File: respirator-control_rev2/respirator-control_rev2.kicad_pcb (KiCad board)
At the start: 2 copper layers, 152 x 152.5 mm, 36 parts, among them J1 Conn_01x02, J2 Header 1X4, J3 Header 1X3, J4 Header 1X3, J5 Header 1X4, J6 Header 1X30, SW1 SW_Push_Dual, SW2 SW_Push, SW3 SW_Push_Dual, U1 LCD-016N002L

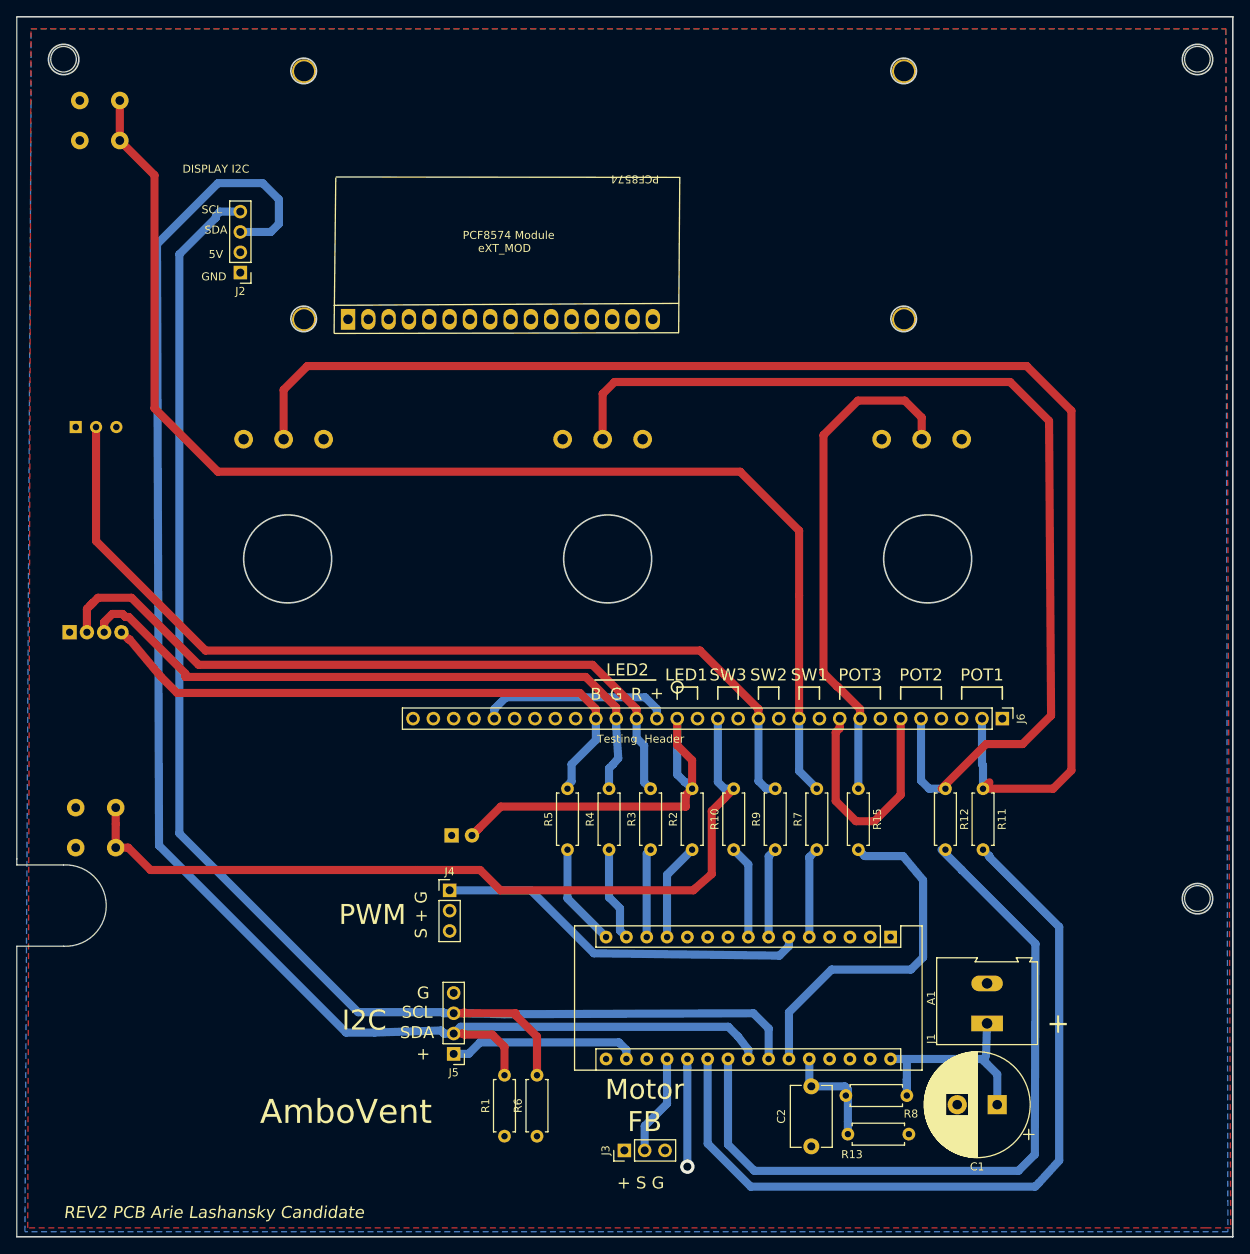
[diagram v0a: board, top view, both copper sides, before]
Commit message: Add files via upload
Change Connectors to horizontal from veritical add Point To secure Cables .
add JPG to Sch to show How to secure Cables.

Gerber in Not Updated  and Not Checked In Fusion  .
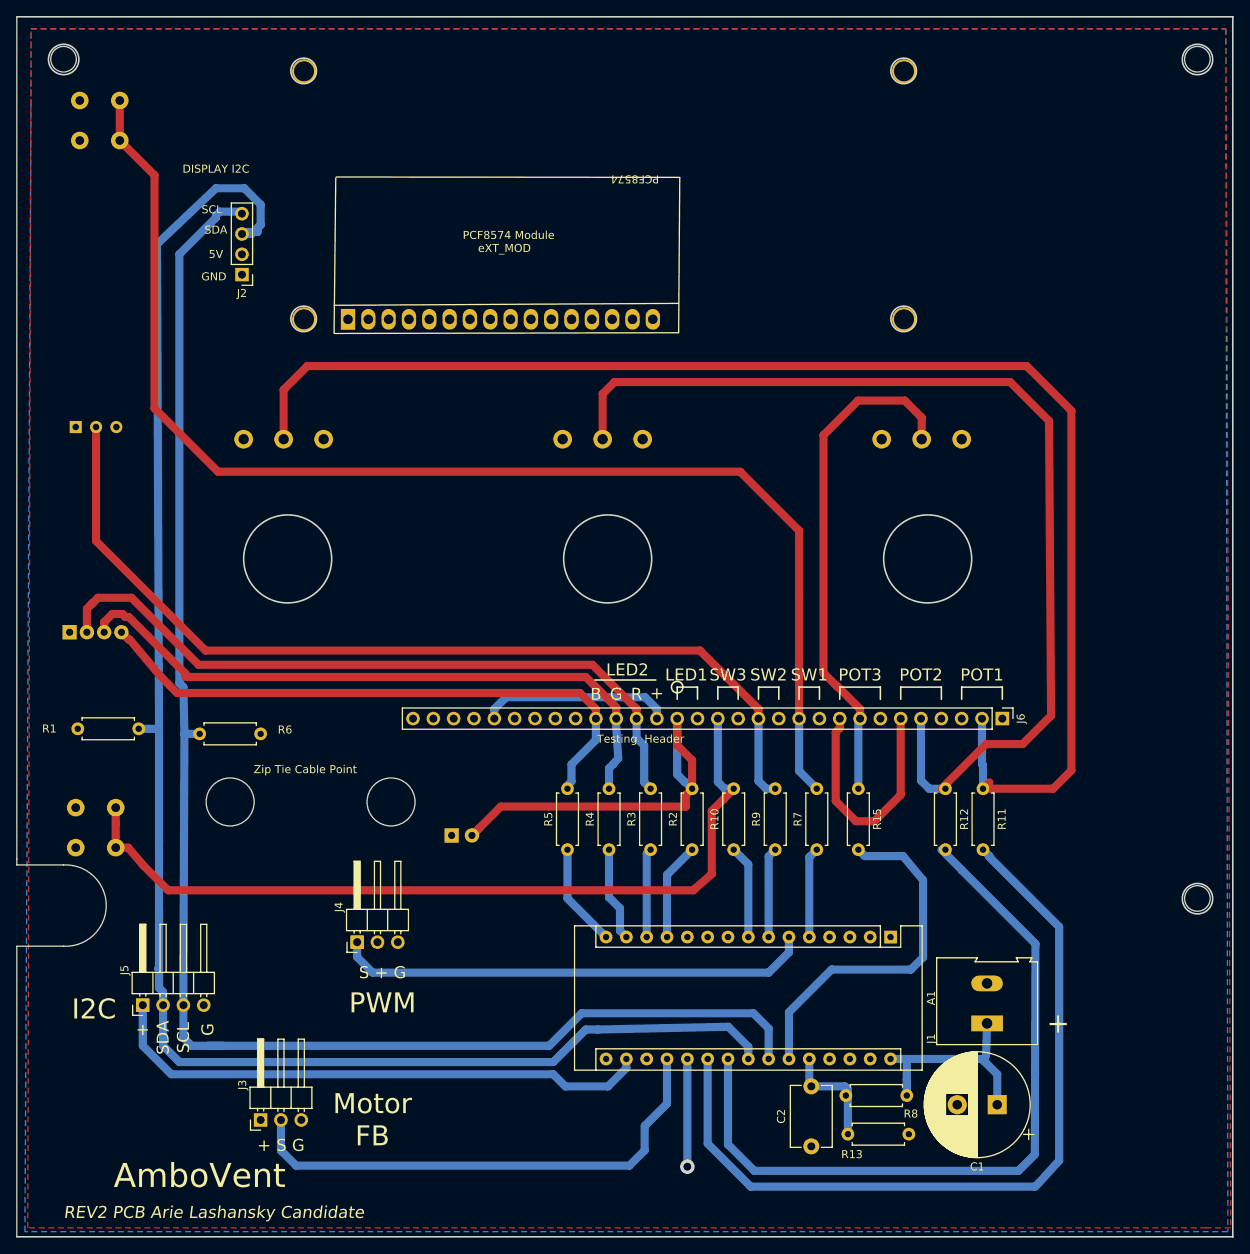
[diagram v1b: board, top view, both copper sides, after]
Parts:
- J3, J4: footprint Connector_PinHeader_2.54mm:PinHeader_1x03_P2.54mm_Vertical -> Connector_PinHeader_2.54mm:PinHeader_1x03_P2.54mm_Horizontal
- J5: footprint Connector_PinHeader_2.54mm:PinHeader_1x04_P2.54mm_Vertical -> Connector_PinHeader_2.54mm:PinHeader_1x04_P2.54mm_Horizontal
- moved R1 73.7 mm to (138.3, 158.5), turned to 0 degrees
- moved R6 61.0 mm to (161.2, 159.1), turned to 180 degrees
- moved J3 45.6 mm to (161.2, 207.4)
- moved J5 39.3 mm to (146.5, 193.0), turned to 90 degrees
- moved J4 13.3 mm to (173.3, 185.2), turned to 90 degrees
- moved J2 0.33 mm to (158.9, 101.7)
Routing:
- net /MOTOR_FB: track 12.6 -> 63.4 mm
- net +3V3: track 23.7 -> 69.7 mm
- net /SDA: track 199.6 -> 218.6 mm
- net /MOTOR_PWM: track 47.3 -> 60.7 mm
- net /SCL: track 186.7 -> 192.4 mm
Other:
- outline, holes or cut-outs redrawn
- board text added: "Zip Tie Cable Point"

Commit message: Add files via upload
Add level convert SCL SDA
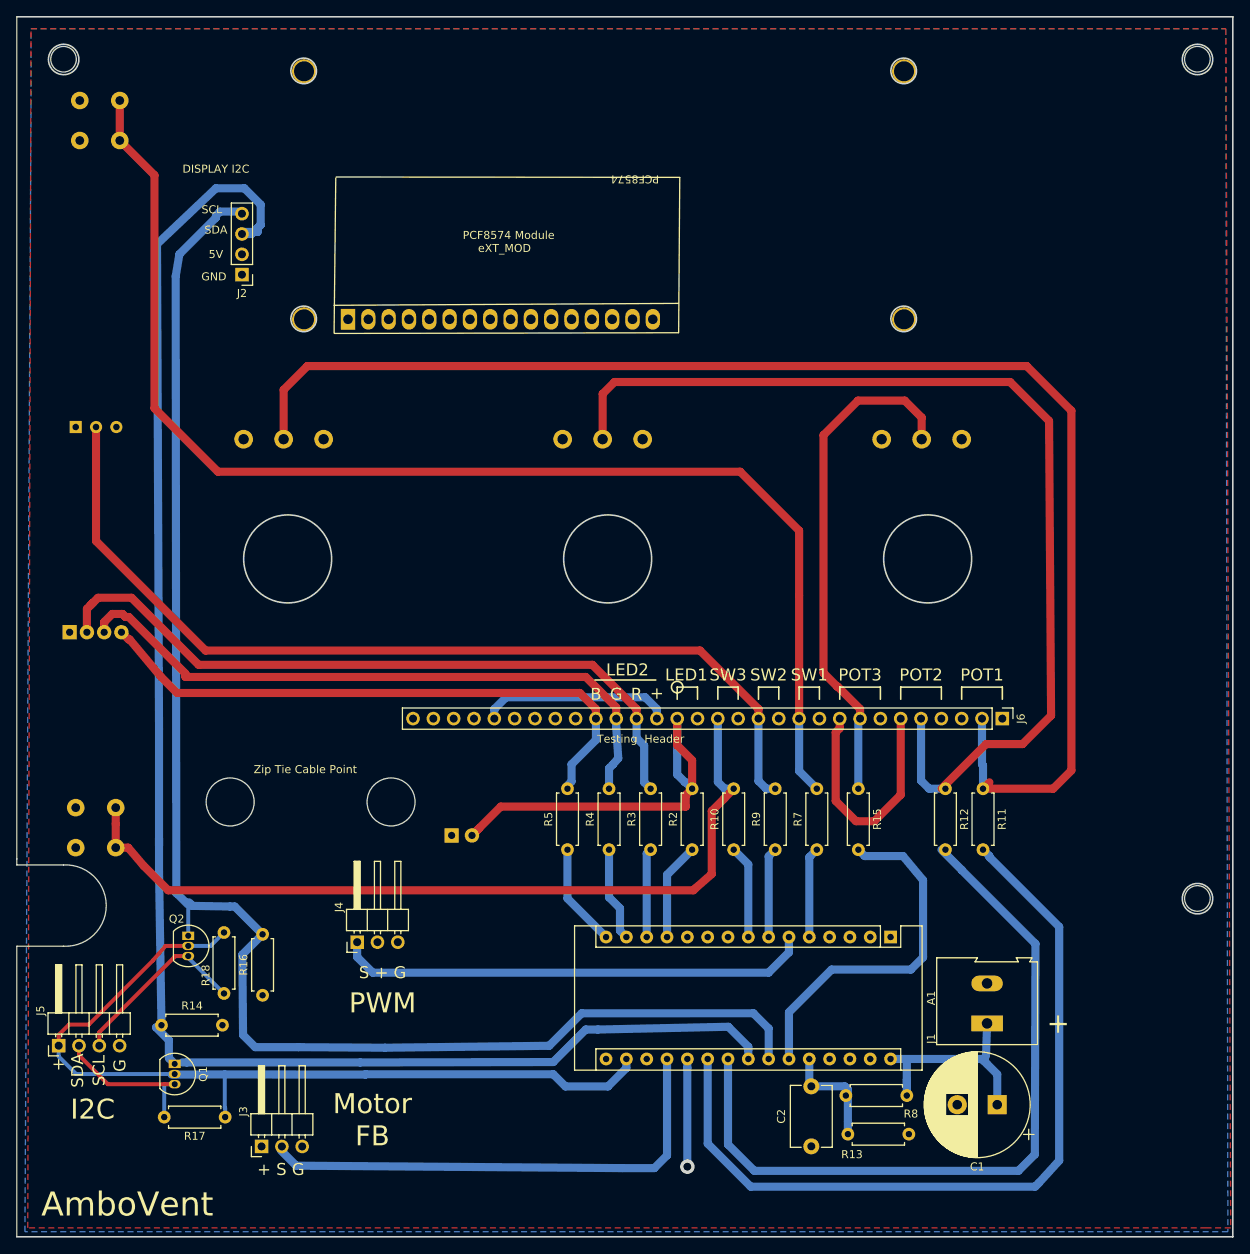
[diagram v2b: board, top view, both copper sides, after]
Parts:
- removed R1, R6: 4.7K, Resistor_THT:R_Axial_DIN0207_L6.3mm_D2.5mm_P7.62mm_Horizontal
- added Q1: 2N7000, Package_TO_SOT_THT:TO-92_Inline, F.Cu at (150.4, 200.4)
- added Q2: 2N7000, Package_TO_SOT_THT:TO-92_Inline, F.Cu at (152.1, 184.4)
- added R14: 10k, Resistor_THT:R_Axial_DIN0207_L6.3mm_D2.5mm_P7.62mm_Horizontal, F.Cu at (156.4, 195.5)
- added R16: 10k, Resistor_THT:R_Axial_DIN0207_L6.3mm_D2.5mm_P7.62mm_Horizontal, F.Cu at (161.4, 191.8)
- added R17: 10k, Resistor_THT:R_Axial_DIN0207_L6.3mm_D2.5mm_P7.62mm_Horizontal, F.Cu at (156.8, 207.0)
- added R18: 10k, Resistor_THT:R_Axial_DIN0207_L6.3mm_D2.5mm_P7.62mm_Horizontal, F.Cu at (156.6, 184.0)
- moved J5 11.7 mm to (135.9, 198.1)
- moved J3 3.32 mm to (161.3, 210.7)
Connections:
- J5 pad 2: /SDA -> /SDA_3V3
- J5 pad 3: /SCL -> /SCL_3V3
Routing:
- net +3V3: track 69.7 -> 109.1 mm
- net /SCL_3V3: track 0.00 -> 23.3 mm
- net /SDA_3V3: track 0.00 -> 20.1 mm
- net /SDA: track 218.6 -> 206.1 mm
- net /MOTOR_FB: track 63.4 -> 61.8 mm
- net /SCL: track 192.4 -> 193.9 mm
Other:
- net class Default: clearance 0.5 -> 0.3
- rule trace_clearance: 0.5 -> 0.3
- board text removed: "REV2 PCB Arie Lashansky Candidate"
